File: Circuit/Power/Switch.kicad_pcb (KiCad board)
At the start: 2 copper layers, 64.8 x 30.5 mm, 30 parts, among them J1 From Control, J2 To Starter, J3 To Capacitor, J4 To Injector, J5 DC In, J6 To Coil Signal, Q1 RFP30N06LE, Q2 RFP30N06LE, Q3 RFP30N06LE, U1 PC817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

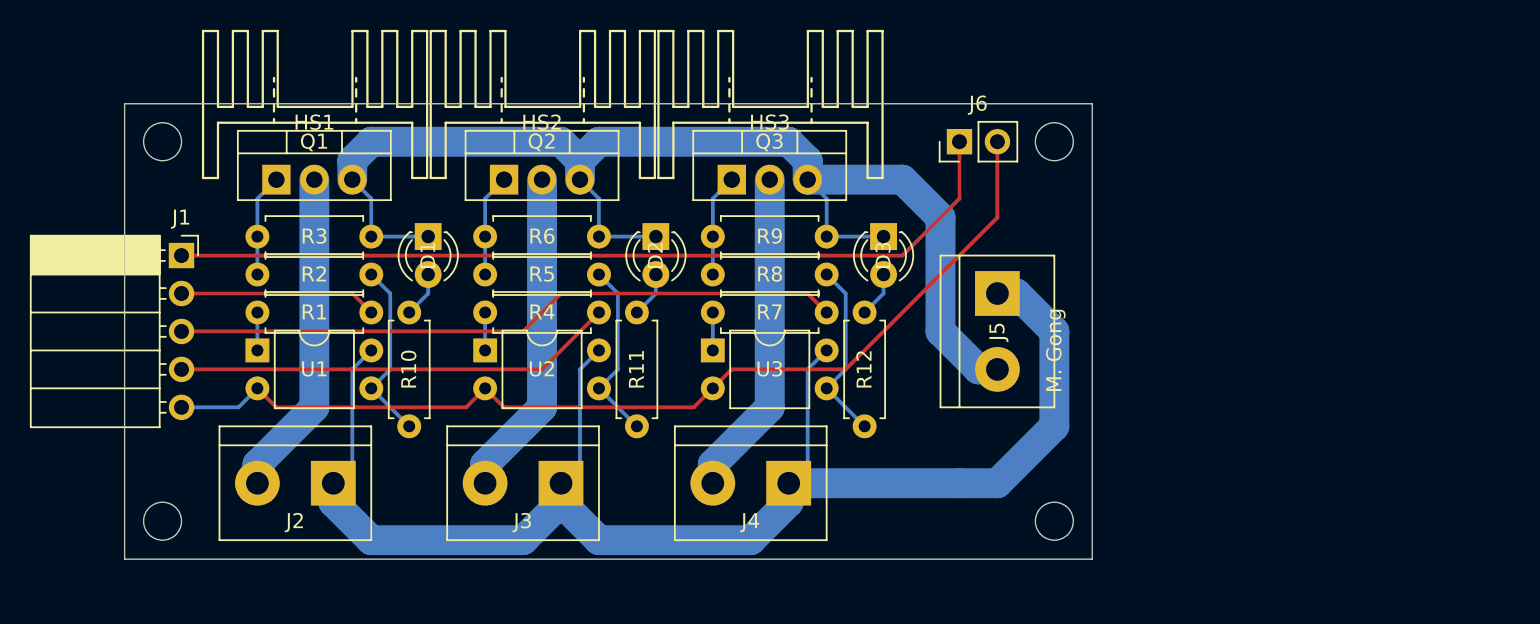
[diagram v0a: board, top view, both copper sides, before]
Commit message: [Circuit] Merge distribution module into switch module
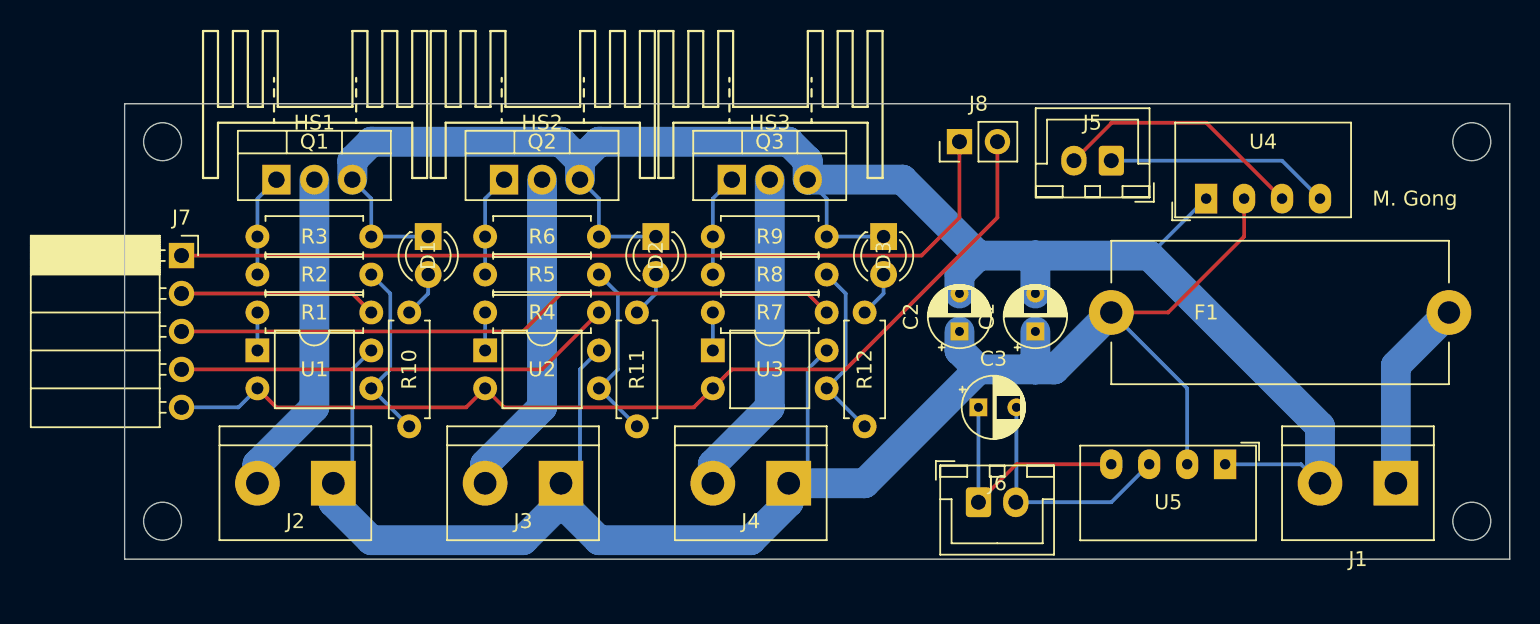
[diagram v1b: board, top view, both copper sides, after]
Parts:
- added C1: 10uF, Capacitor_THT:CP_Radial_D4.0mm_P2.00mm, F.Cu at (135.9, 85.1)
- added C2: 2.2uF, Capacitor_THT:CP_Radial_D4.0mm_P2.00mm, F.Cu at (130.8, 85.1)
- added C3: 2.2uF, Capacitor_THT:CP_Radial_D4.0mm_P2.00mm, F.Cu at (132.1, 90.2)
- added F1: Fuse, Fuse:Fuseholder_Cylinder-5x20mm_Stelvio-Kontek_PTF78_Horizontal_Open, F.Cu at (141.0, 83.8)
- added J1: Main Power In, TerminalBlock:TerminalBlock_bornier-2_P5.08mm, F.Cu at (160.0, 95.2)
- added J6: To Control Power, Connector_JST:JST_XH_B2B-XH-A_1x02_P2.50mm_Vertical, F.Cu at (132.1, 96.5)
- added U4: B1212S, Converter_DCDC:Converter_DCDC_muRata_CRE1xxxxxxSC_THT, F.Cu at (147.3, 76.2)
- added U5: B1212S, Converter_DCDC:Converter_DCDC_muRata_CRE1xxxxxxSC_THT, F.Cu at (148.6, 94.0)
- J5: value DC In -> To Coil; footprint TerminalBlock:TerminalBlock_bornier-2_P5.08mm -> Connector_JST:JST_XH_B2B-XH-A_1x02_P2.50mm_Vertical
- moved J5 11.7 mm to (141.0, 73.7), turned to 180 degrees
- renumbered J1 to J7, J6 to J8
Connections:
- D1 pad 1: /PowerDC-In -> /PowerIn-
- D2 pad 1: /PowerDC-In -> /PowerIn-
- D3 pad 1: /PowerDC-In -> /PowerIn-
- J5 pad 1: /CapacitorPower+ -> /CoilPower+
- J5 pad 2: /PowerDC-In -> /CoilPower-
- Q1 pad 3: /PowerDC-In -> /PowerIn-
- Q2 pad 3: /PowerDC-In -> /PowerIn-
- Q3 pad 3: /PowerDC-In -> /PowerIn-
- R3 pad 2: /PowerDC-In -> /PowerIn-
- R6 pad 2: /PowerDC-In -> /PowerIn-
- R9 pad 2: /PowerDC-In -> /PowerIn-
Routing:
- net /PowerIn-: track 0.00 -> 123.6 mm
- net /PowerDC-In: track 83.3 -> 0.00 mm
- net /CapacitorPower+: track 98.9 -> 126.1 mm
- net /CoilPower-: track 0.00 -> 17.1 mm
- net /ControlPower-: track 0.00 -> 16.3 mm
- net /ControlPower+: track 0.00 -> 16.3 mm
- net /CoilPower+: track 0.00 -> 15.0 mm
- net /PowerIn+: track 0.00 -> 12.9 mm
- net /CoilSignal: track 57.5 -> 58.2 mm
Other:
- board size 64.8 x 30.5 mm -> 92.7 x 30.5 mm

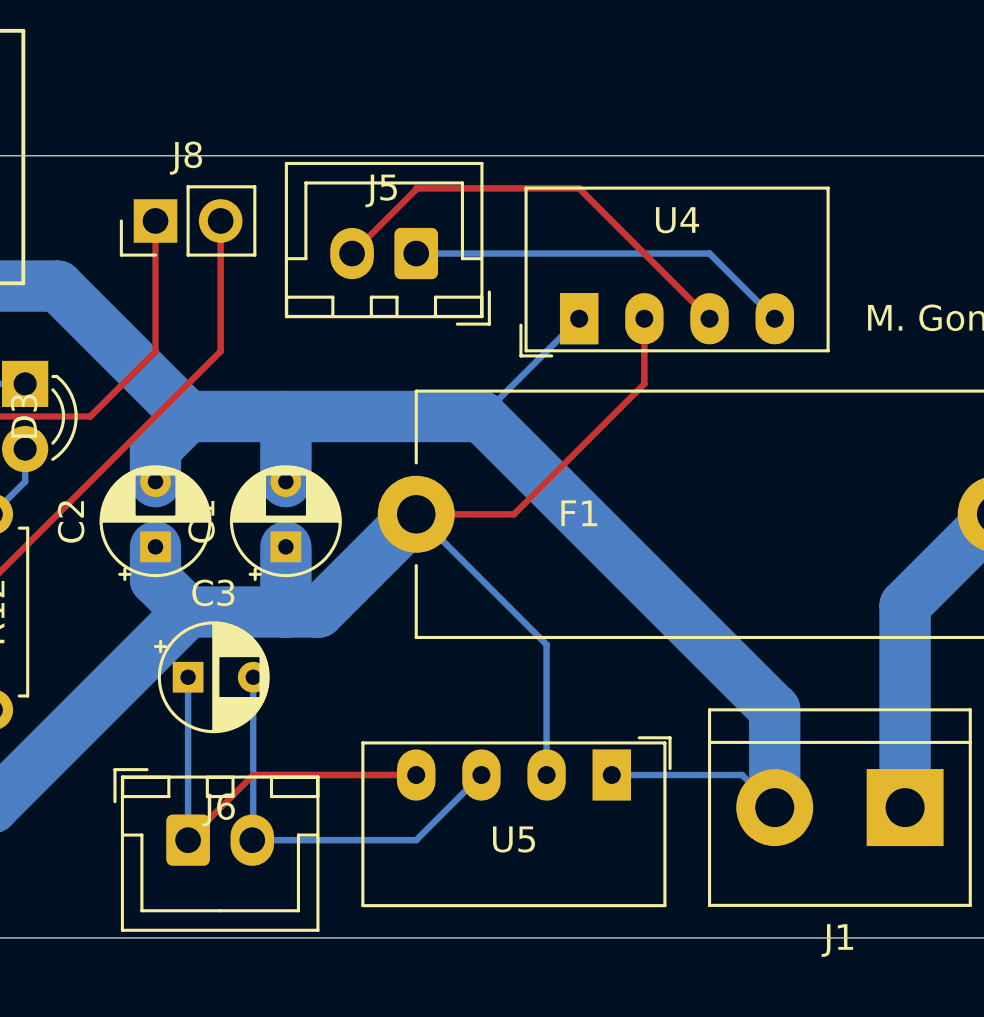
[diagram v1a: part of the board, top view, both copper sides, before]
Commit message: [Circuit] Add an LED indicator for power input
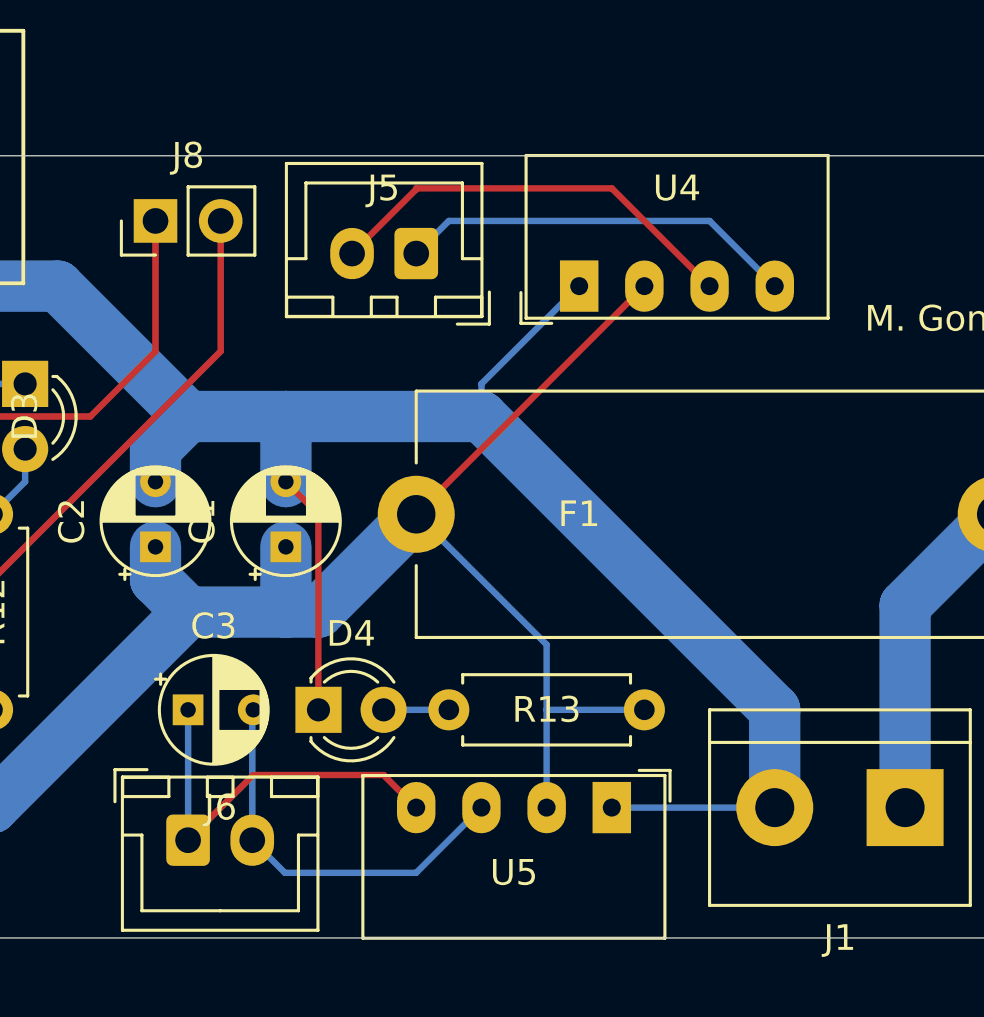
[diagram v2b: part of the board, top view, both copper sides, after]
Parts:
- added D4: LED, LED_THT:LED_D3.0mm_FlatTop, F.Cu at (137.2, 91.4)
- added R13: 2.2K, Resistor_THT:R_Axial_DIN0207_L6.3mm_D2.5mm_P7.62mm_Horizontal, F.Cu at (149.9, 91.4)
- moved C3 1.27 mm to (132.1, 91.4)
- moved U4 1.27 mm to (147.3, 74.9)
- moved U5 1.27 mm to (148.6, 95.2)
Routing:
- net /PowerIn-: track 123.6 -> 133.8 mm
- net /CapacitorPower+: track 126.1 -> 130.2 mm
- net Net-(D4-Pad2): track 0.00 -> 2.54 mm
- net /ControlPower+: track 16.3 -> 15.5 mm
- net /ControlPower-: track 16.3 -> 15.7 mm
- net /CoilPower-: track 17.1 -> 16.6 mm
- net /CoilPower+: track 15.0 -> 15.5 mm

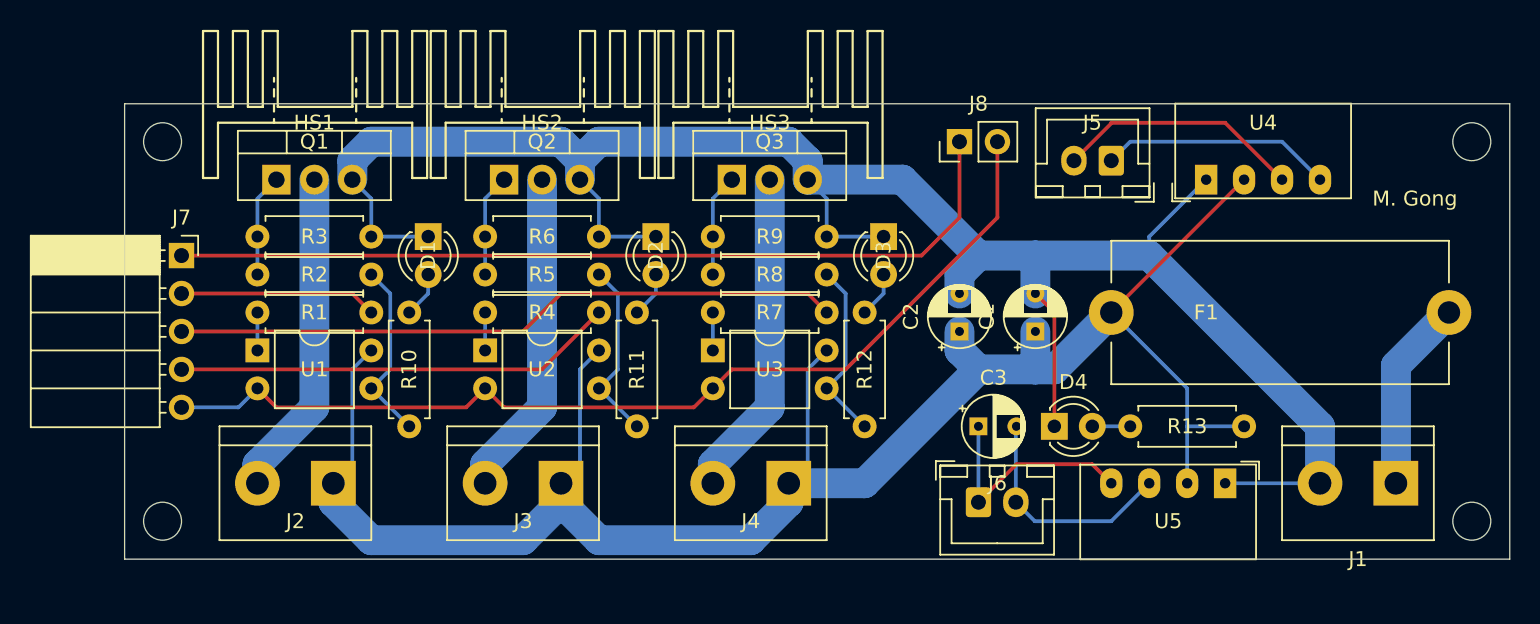
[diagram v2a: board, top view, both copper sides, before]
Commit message: [Circuit] Fine tune the PCB of switch module
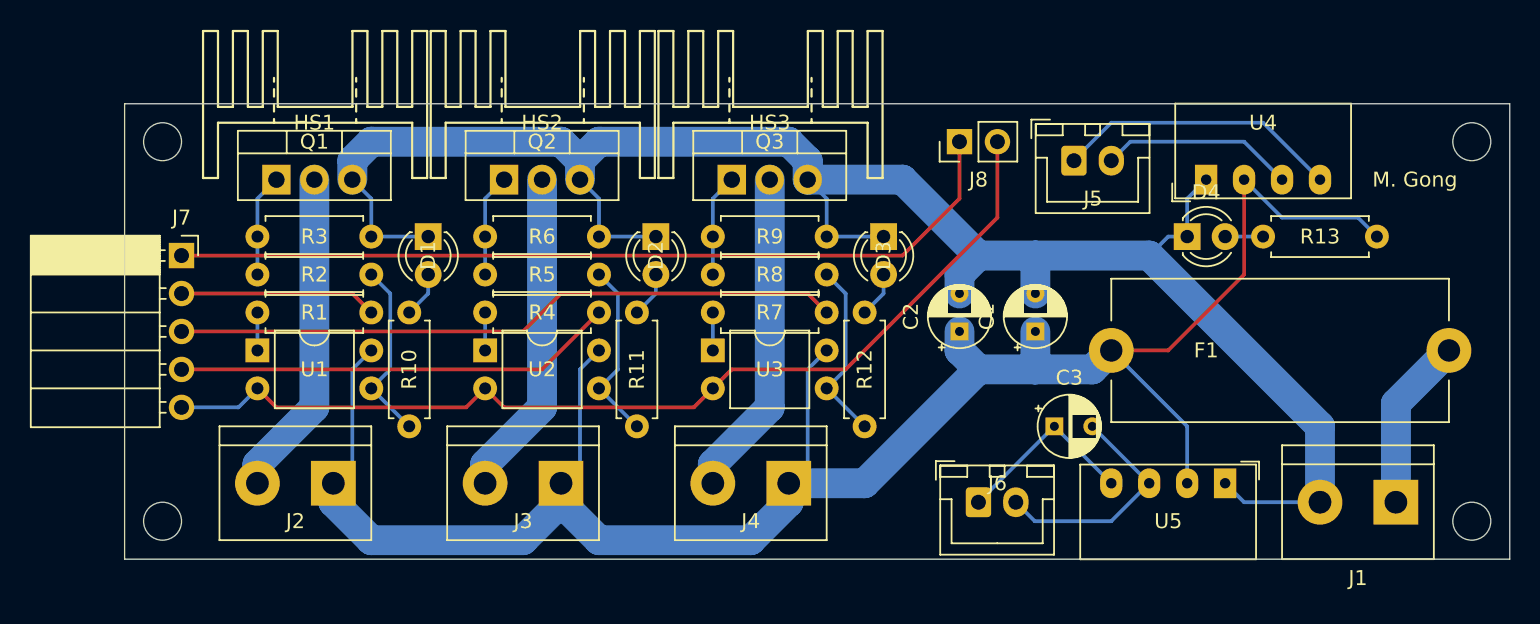
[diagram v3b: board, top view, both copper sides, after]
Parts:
- moved D4 15.5 mm to (146.1, 78.7)
- moved R13 15.5 mm to (158.8, 78.7)
- moved C3 5.08 mm to (137.2, 91.4)
- moved F1 2.54 mm to (141.0, 86.4)
- moved J5 2.50 mm to (138.5, 73.7), turned to 0 degrees
- moved J1 1.27 mm to (160.0, 96.5)
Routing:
- net /CapacitorPower+: track 130.2 -> 139.3 mm
- net /PowerIn-: track 133.8 -> 126.9 mm
- net /CoilPower-: track 16.6 -> 13.0 mm
- net /CoilPower+: track 15.5 -> 19.1 mm
- net /ControlPower+: track 15.5 -> 12.6 mm
- net /PowerIn+: track 12.9 -> 11.6 mm
- net /CoilSignal: track 58.2 -> 57.5 mm

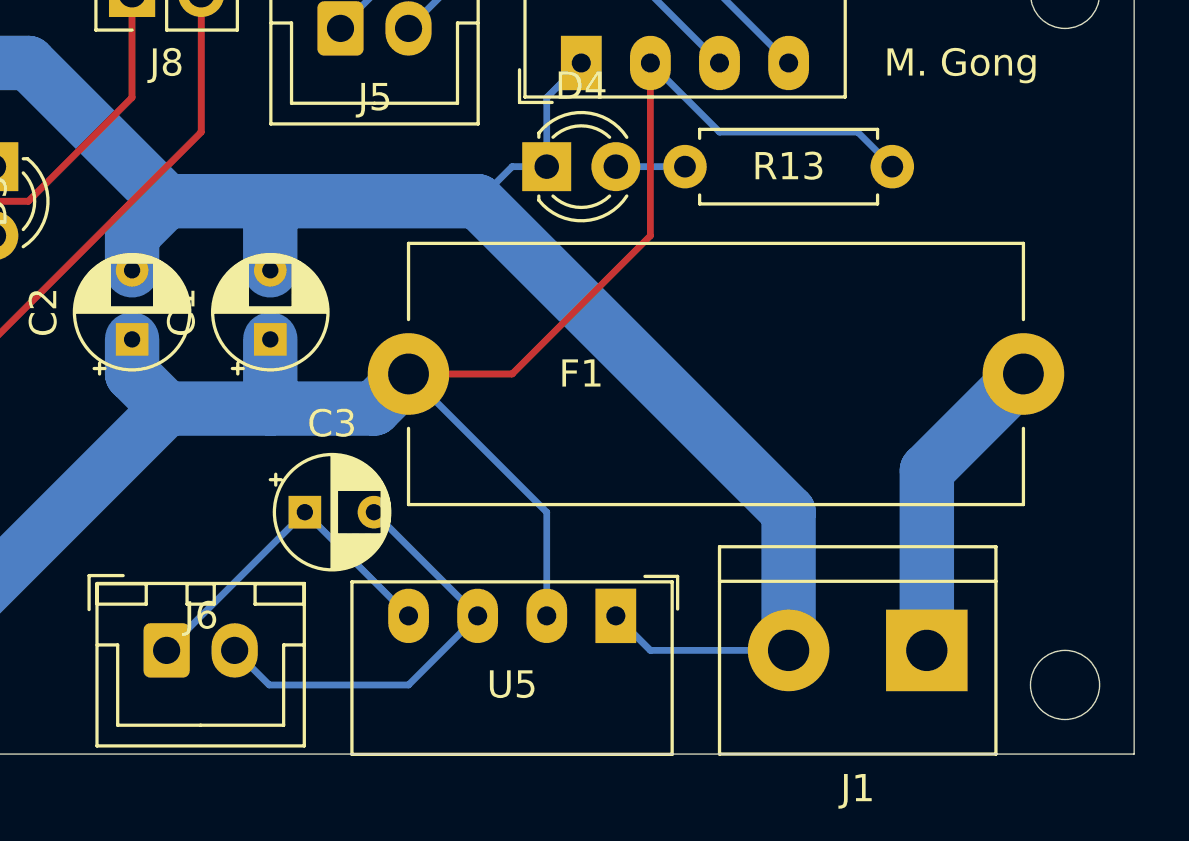
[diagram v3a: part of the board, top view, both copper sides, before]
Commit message: [Circuit] Change the footprint of fuse holder based on the measurement
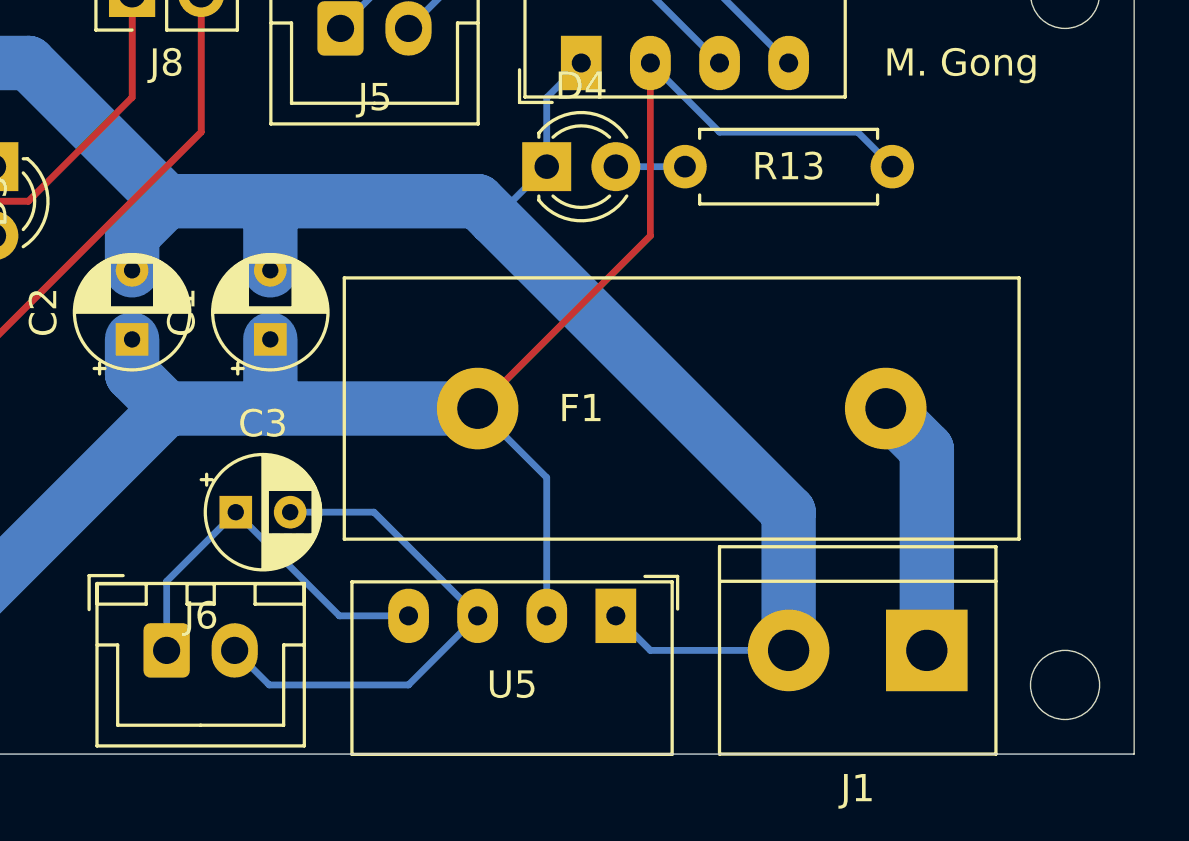
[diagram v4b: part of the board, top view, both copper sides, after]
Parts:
- F1: footprint Fuse:Fuseholder_Cylinder-5x20mm_Stelvio-Kontek_PTF78_Horizontal_Open -> Power:Fuseholder_Cylinder-5x20mm_ASI_PTF-76-10_Horizontal_Open
- moved F1 2.84 mm to (143.5, 87.6)
- moved C3 2.54 mm to (134.6, 91.4)
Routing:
- net /CapacitorPower+: track 139.3 -> 135.7 mm
- net /ControlPower-: track 16.0 -> 19.0 mm
- net /PowerIn+: track 11.6 -> 9.52 mm
- net /ControlPower+: track 12.6 -> 14.1 mm

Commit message: [Circuit] Use 5V power for control module
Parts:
- C3: value 2.2uF -> 10uF
- U5: value B1212S -> B1205S
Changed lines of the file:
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@@
       (effects (font (size 1 1) (thickness 0.15)))
     )
-    (fp_text value 2.2uF (at 1 3.25) (layer F.Fab)
+    (fp_text value 10uF (at 1 3.25) (layer F.Fab)
       (effects (font (size 1 1) (thickness 0.15)))
     )
@@
       (effects (font (size 1 1) (thickness 0.15)))
     )
-    (fp_text value B1212S (at 3.81 3.81 180) (layer F.Fab)
-      (effects (font (size 1 1) (thickness 0.15)))
-    )
+    (fp_text value B1205S (at 3.81 3.81 180) (layer F.Fab)
+      (effects (font (size 1 1) (thickness 0.15)))
+    )
